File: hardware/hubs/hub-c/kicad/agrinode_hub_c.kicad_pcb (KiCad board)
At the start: 2 copper layers, 130 x 96 mm, 119 parts, among them J1 DC 12V 5.5/2.1, J10 LTE MODULE, J2 DC IN 7-24V, J3 SOLAR 6-24V, J4 USB 5V / PROG, J5 BAT NTC 10k, J6 PROG, J7 I2C, J8 LED STRIP WS2813, J9 RS-485, Q1 AO3401A, Q2 AO3401A, Q3 MMBT3904, Q4 MMBT3904, Q5 BSS138, Q6 MMBT3904, Q7 AO3401A, Q8 MMBT3904, Q9 MMBT3904, SW1 RESET, SW2 BOOT / PAIR, U1 LM2596S-5.0, U2 TP4056, U3 MIC29302WU, U4 ESP32-WROOM-32E-N8, U5 CH340C, U6 DS3231MZ, U7 MAX3485ESA, U8 MIC29302WU

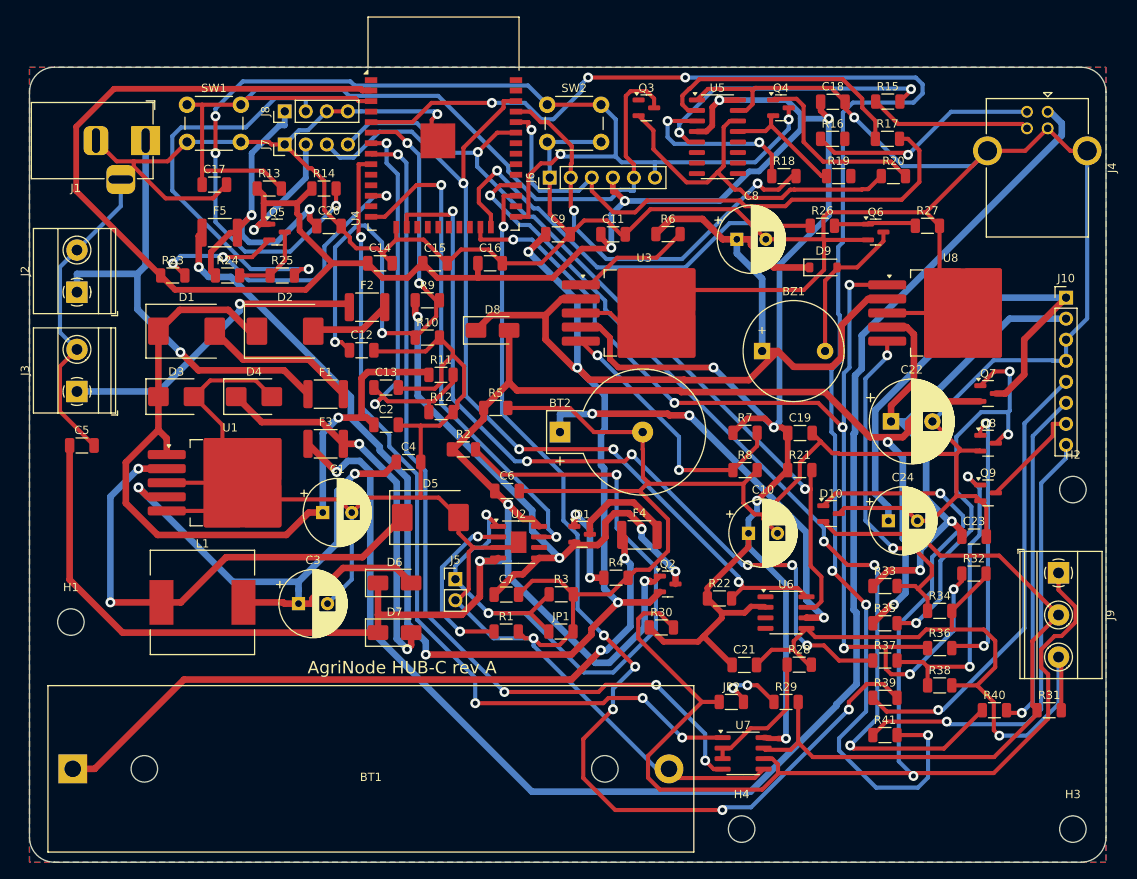
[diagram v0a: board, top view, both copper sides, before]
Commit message: hubs: intermediate routed boards (HUB-W 1 open connection; others in progress)
Co-Authored-By: Claude Opus 5.5 <noreply@anthropic.com>
Claude-Session: https://claude.ai/code/session_014J7amXZ5Y6AZWEh5CjDNja
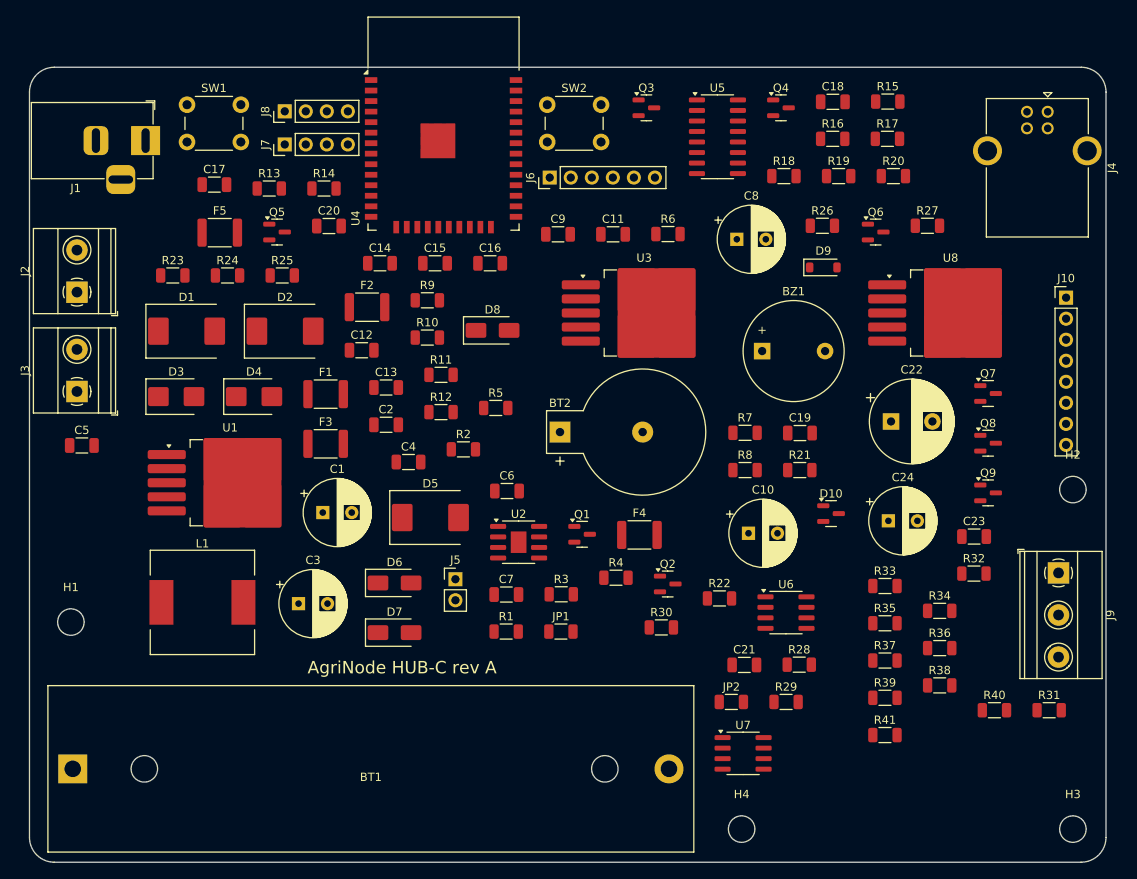
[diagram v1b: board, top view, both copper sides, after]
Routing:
- net GND: track 887.1 -> 0.00 mm, vias 4 -> 0
- net +3V3: track 375.5 -> 0.00 mm, vias 9 -> 0
- net VSYS: track 253.2 -> 0.00 mm, vias 5 -> 0
- net V5: track 243.3 -> 0.00 mm, vias 5 -> 0
- net MODEM_STATUS: track 186.1 -> 0.00 mm, vias 6 -> 0
- net /Power - 12V, solar and USB inputs, 18650 charger, rails/VUSB_RAW: track 182.0 -> 0.00 mm, vias 1 -> 0
- net /RS-485 and uplink/RS485_A: track 163.3 -> 0.00 mm, vias 2 -> 0
- net MODEM_EN: track 135.8 -> 0.00 mm, vias 7 -> 0
- net /ESP32, programming, buttons, RTC, LED strip, buzzer/BOOT_BTN: track 135.6 -> 0.00 mm, vias 5 -> 0
- net MODEM_RXD: track 128.2 -> 0.00 mm, vias 6 -> 0
- net /ESP32, programming, buttons, RTC, LED strip, buzzer/ESP_EN: track 114.4 -> 0.00 mm
- net /ESP32, programming, buttons, RTC, LED strip, buzzer/I2C_SCL: track 114.0 -> 0.00 mm, vias 4 -> 0
- net MODEM_TXD: track 111.4 -> 0.00 mm, vias 4 -> 0
- net RS485_TX: track 106.3 -> 0.00 mm, vias 4 -> 0
- net RS485_RX: track 104.5 -> 0.00 mm, vias 4 -> 0
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- removed copper zone on B.Cu, net GND
- removed copper zone on F.Cu, net GND

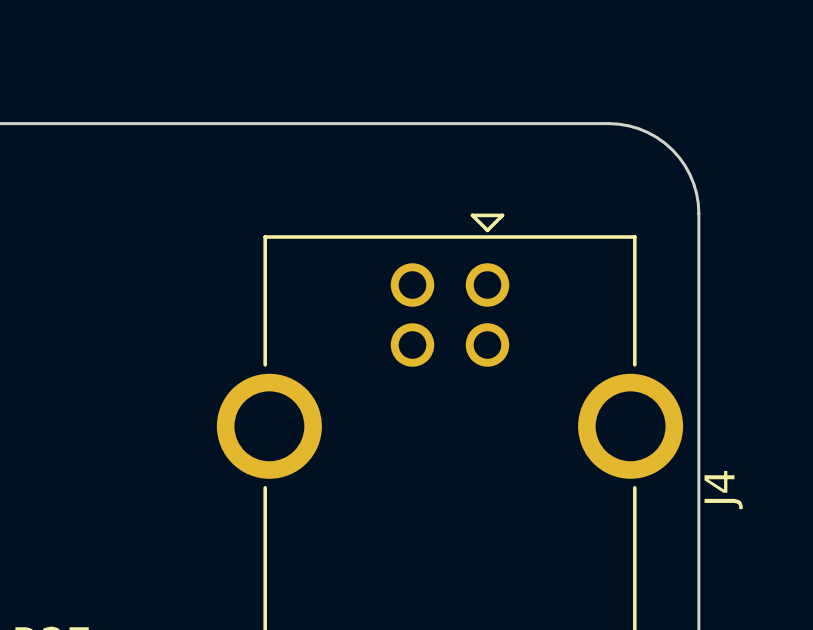
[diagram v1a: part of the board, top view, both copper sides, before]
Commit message: hubs: boards after GPIO remap (placement; routing in progress)
Co-Authored-By: Claude Opus 5.5 <noreply@anthropic.com>
Claude-Session: https://claude.ai/code/session_014J7amXZ5Y6AZWEh5CjDNja
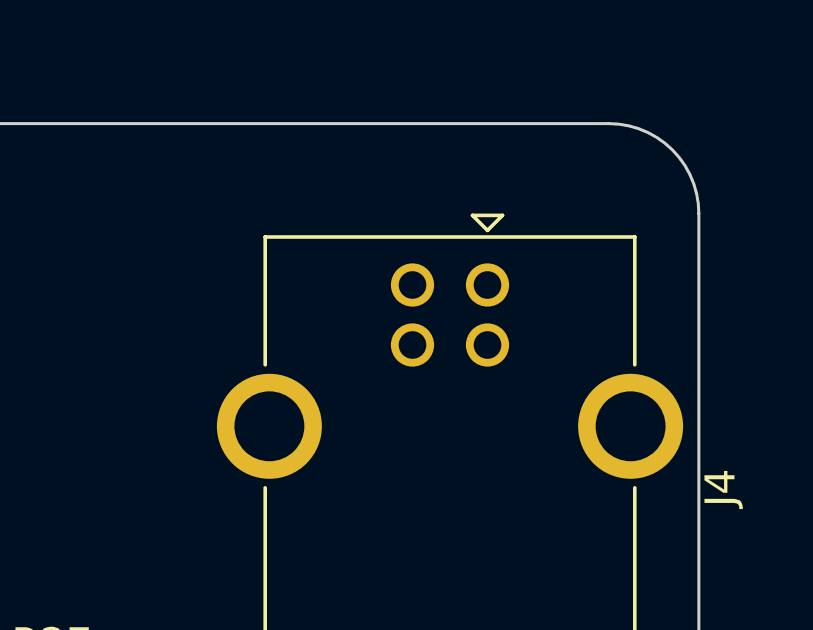
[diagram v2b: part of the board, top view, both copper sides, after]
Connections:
- U4 pad 10: RS485_DE -> unconnected-(U4-IO25-Pad10)
- U4 pad 14: CHRG_N -> unconnected-(U4-IO12-Pad14)
- U4 pad 16: MODEM_PWRKEY_CTL -> CHRG_N
- U4 pad 23: MODEM_EN -> unconnected-(U4-IO15-Pad23)
- U4 pad 26: unconnected-(U4-IO4-Pad26) -> RS485_DE
- U4 pad 27: MODEM_RXD -> RS485_RX
- U4 pad 28: MODEM_TXD -> RS485_TX
- U4 pad 30: unconnected-(U4-IO18-Pad30) -> MODEM_STATUS
- U4 pad 31: unconnected-(U4-IO19-Pad31) -> MODEM_RXD
- U4 pad 33: /ESP32, programming, buttons, RTC, LED strip, buzzer/I2C_SDA -> MODEM_PWRKEY_CTL
- U4 pad 36: /ESP32, programming, buttons, RTC, LED strip, buzzer/I2C_SCL -> MODEM_EN
- U4 pad 37: unconnected-(U4-IO23-Pad37) -> MODEM_TXD
- U4 pad 5: MODEM_STATUS -> unconnected-(U4-SENSOR_VN-Pad5)
- U4 pad 8: RS485_TX -> /ESP32, programming, buttons, RTC, LED strip, buzzer/I2C_SCL
- U4 pad 9: RS485_RX -> /ESP32, programming, buttons, RTC, LED strip, buzzer/I2C_SDA
